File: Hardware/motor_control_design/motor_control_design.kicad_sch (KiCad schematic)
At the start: 78 parts, among them J10 3V3, J2 SWD, J3 VBAT, J4 GND, J5 FC_M/P, J6 Conn_01x06, J8 Conn_01x06, J9 GND, Q1 RF1S9540SM, Q10 2N7002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

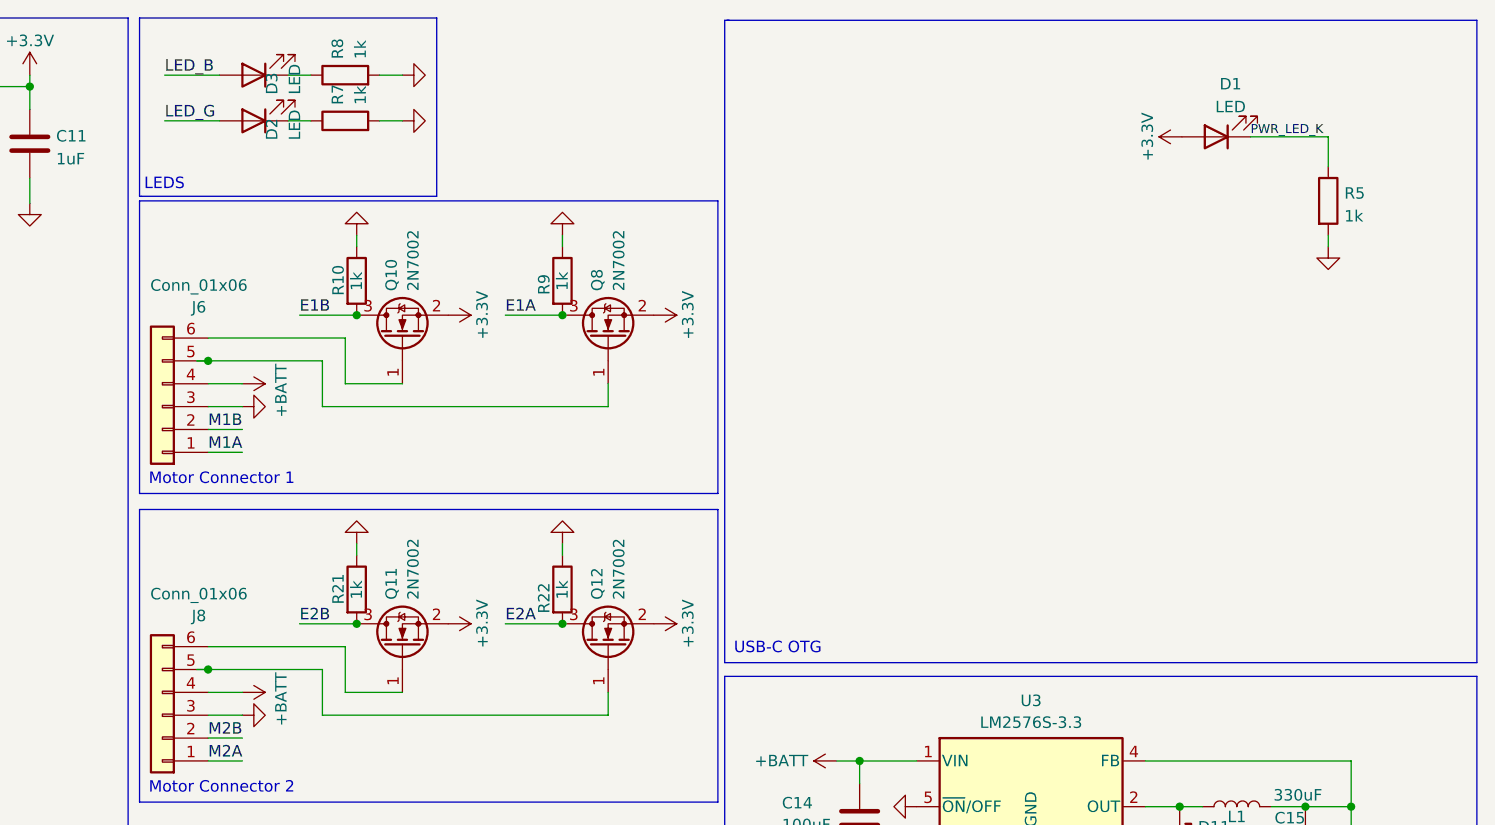
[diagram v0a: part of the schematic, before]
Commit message: Cleaned up motor board schema
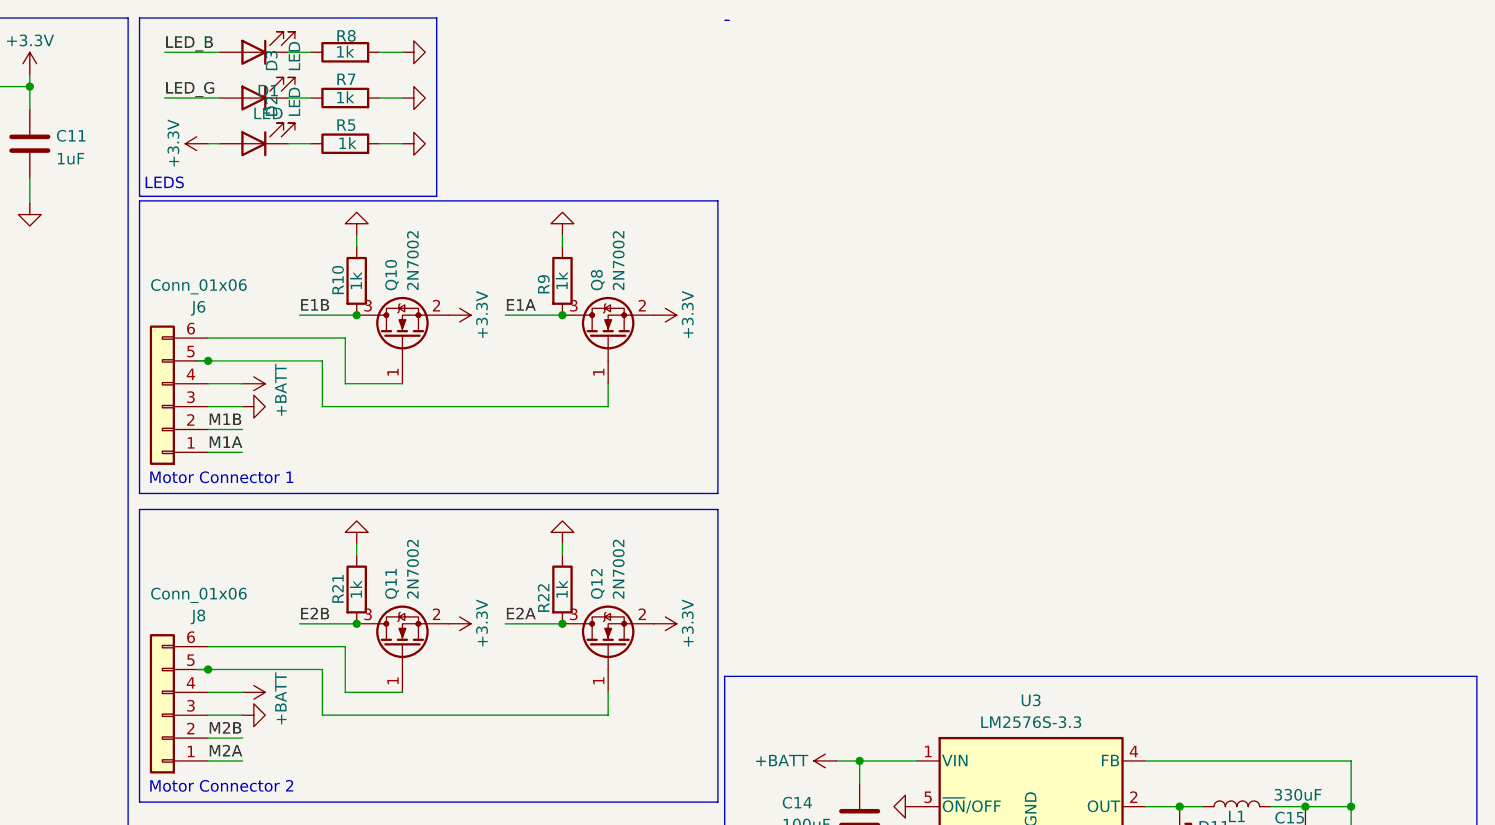
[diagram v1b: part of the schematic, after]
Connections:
- net PWR_LED_K: no longer names the net of D1.1 (K), R5.1
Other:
- note removed: "USB-C OTG"
- moved on the sheet: D1, D2, D3, R5, R7, R8

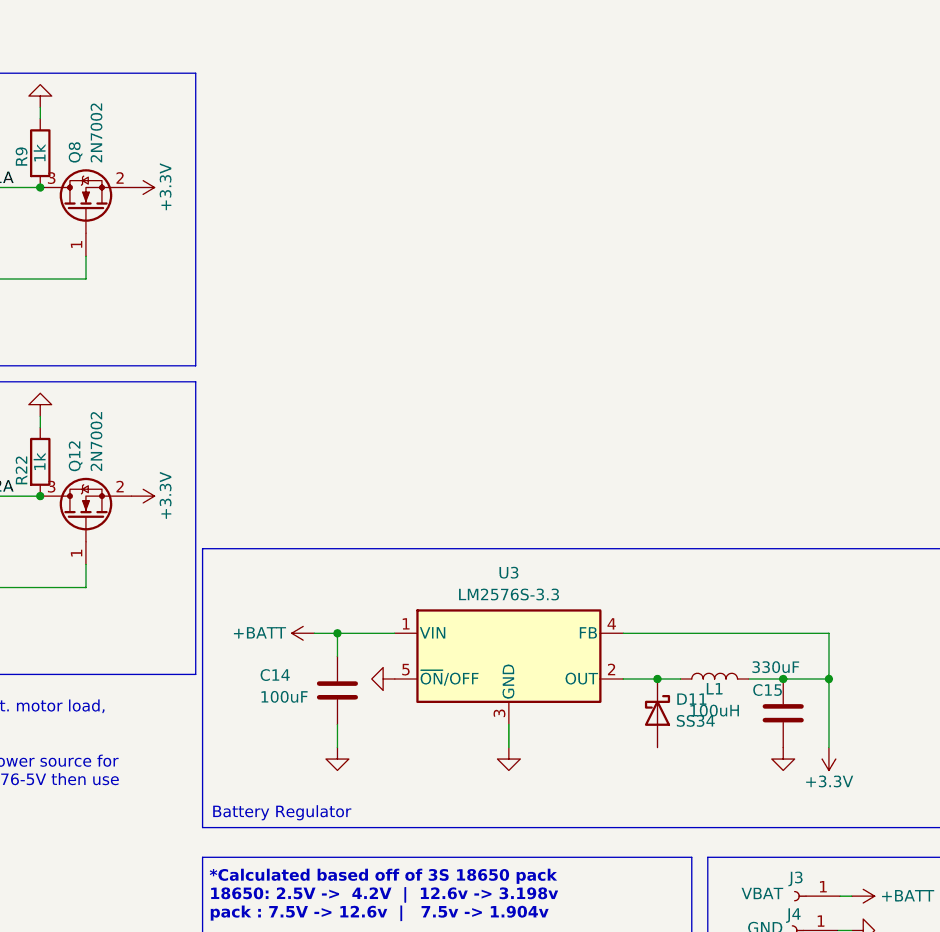
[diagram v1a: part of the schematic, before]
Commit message: Motor Board: Added LCSC Part Numbers Fixed missing ground on diode
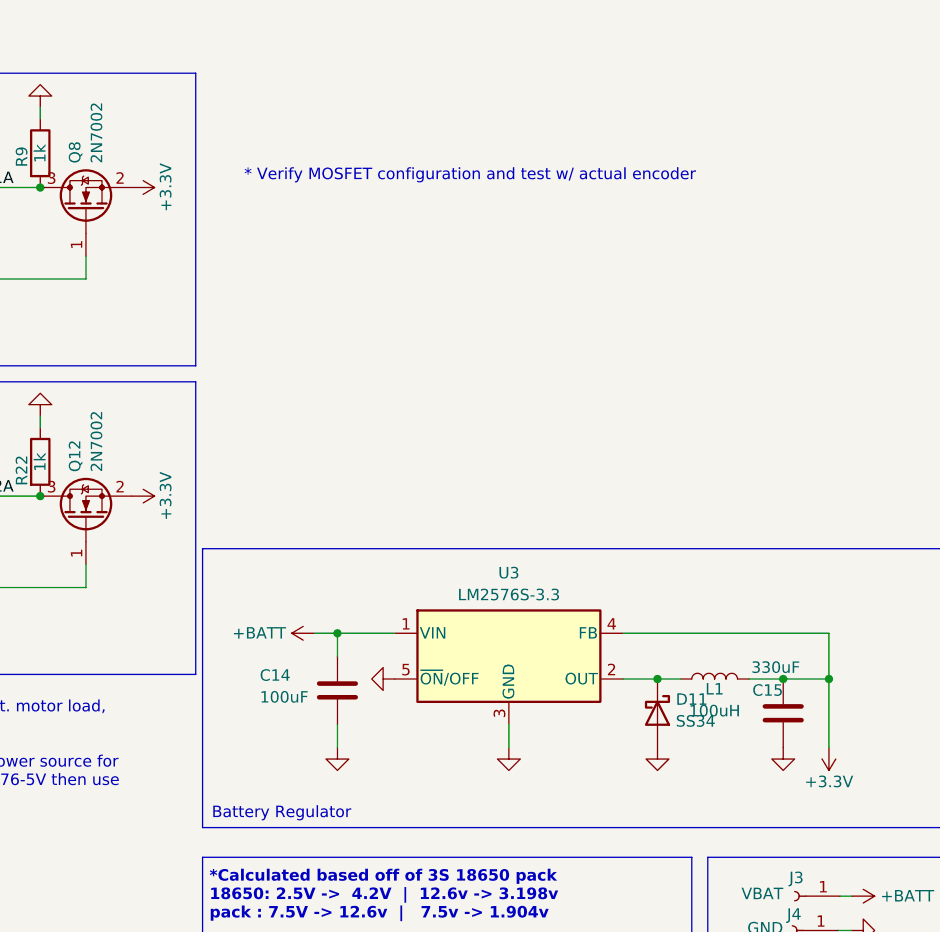
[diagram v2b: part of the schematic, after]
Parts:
- J5: LCSC Part (none) -> C124378
- Q1, Q14, Q2, Q6: LCSC Part (none) -> C33903
- Q10, Q11, Q12, Q13, Q16, Q4, Q5, Q8: LCSC Part (none) -> C466660
- Q15, Q3, Q7, Q9: LCSC Part (none) -> C538199
- R1, R2: LCSC Part C25906 -> C174364
- R10, R21, R22, R5, R7, R8, R9: LCSC Part C11702 -> C102758
- R11: LCSC Part C25906 -> C162880
- R12: LCSC Part C25906 -> C176114
- R13, R14, R15, R16, R17, R18, R19, R20, R23, R24, R4, R6: LCSC Part C60490 -> C102758
- R3: LCSC Part C60490 -> C176114
- U3: LCSC Part (none) -> C347414
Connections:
- net GND: now also D11.2 (A)
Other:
- note added: "* Verify MOSFET configuration and test w/ actual encoder"

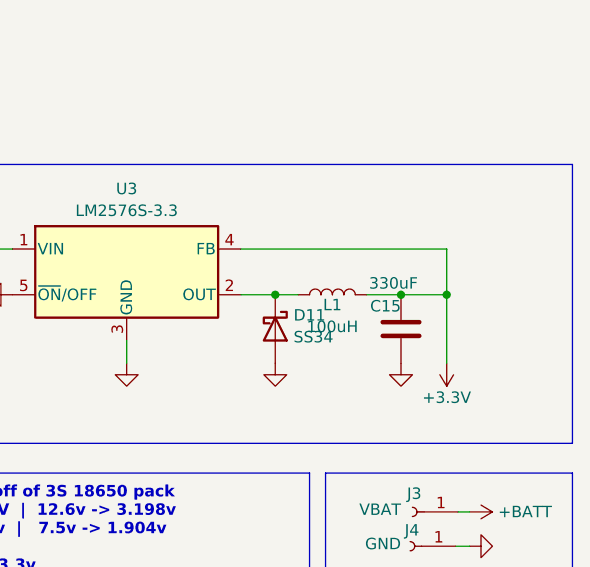
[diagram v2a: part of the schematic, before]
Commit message: Motor Board: Optimized LM2576 circuit - bigger capacitor - better inductor Added assembly files (outdated)
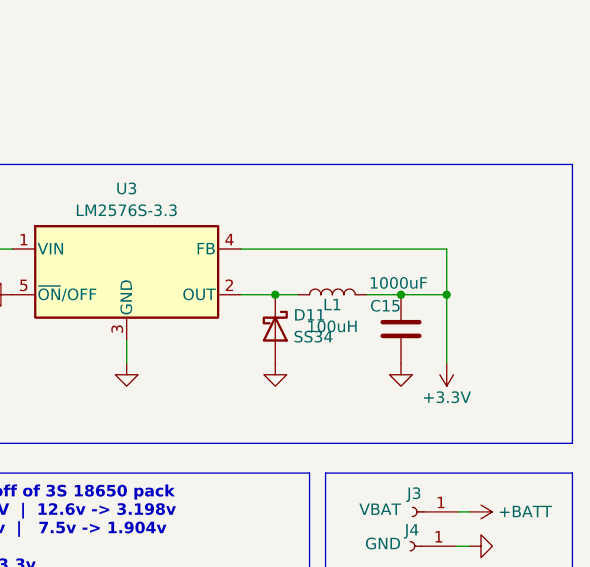
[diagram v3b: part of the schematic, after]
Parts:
- C14: footprint Capacitor_SMD:C_0603_1608Metric -> Capacitor_SMD:C_0805_2012Metric; LCSC Part C19702 -> C141660
- C15: value 330uF -> 1000uF; footprint Capacitor_SMD:C_0402_1005Metric -> Capacitor_SMD:CP_Elec_10x10.5; LCSC Part C19702 -> C189257
- D1: LCSC Part C273598 -> C2286
- D10, D11, D12, D4, D5, D6, D7, D8, D9: LCSC Part (none) -> C3032484
- D2: LCSC Part C273598 -> C779453
- D3: LCSC Part C273598 -> C131286
- J5: LCSC Part C124378 -> C132510
- L1: footprint Inductor_SMD:L_12x12mm_H4.5mm -> Inductor_SMD:L_TaiTech_TMPC1265_13.5x12.5mm; LCSC Part (none) -> C408533
- U3: LCSC Part C347414 -> C347412
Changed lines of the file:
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@@
 			)
 		)
+		(property "LCSC Part" "C3032484"
+			(at 124.46 153.67 90)
+			(effects
+				(font
+					(size 1.27 1.27)
+				)
+				(hide yes)
+			)
+		)
 		(pin "1"
 		)
@@
 			)
 		)
-		(property "LCSC Part" "C124378"
+		(property "LCSC Part" "C132510"
 			(at 275.59 148.59 0)
 			(effects
@@
 			)
 		)
-		(property "LCSC Part" "C273598"
+		(property "LCSC Part" "C2286"
 			(at 146.05 27.94 0)
 			(effects
@@
 			)
 		)
-		(property "Value" "330uF"
+		(property "Value" "1000uF"
 			(at 259.334 100.33 0)
 			(effects
@@
 			)
 		)
-		(property "Footprint" "Capacitor_SMD:C_0402_1005Metric"
+		(property "Footprint" "Capacitor_SMD:CP_Elec_10x10.5"
 			(at 263.8552 101.6 0)
 			(effects
@@
 			)
 		)
-		(property "LCSC Part" "C19702"
+		(property "LCSC Part" "C189257"
 			(at 262.89 105.41 0)
 			(effects
@@
 			)
 		)
+		(property "LCSC Part" "C3032484"
+			(at 59.69 166.37 90)
+			(effects
+				(font
+					(size 1.27 1.27)
+				)
+				(hide yes)
+			)
+		)
 		(pin "1"
 		)
@@
 			)
 		)
+		(property "LCSC Part" "C3032484"
+			(at 44.45 153.67 90)
+			(effects
+				(font
+					(size 1.27 1.27)
+				)
+				(hide yes)
+			)
+		)
 		(pin "1"
 		)
@@
 			)
 		)
+		(property "LCSC Part" "C3032484"
+			(at 124.46 166.37 90)
+			(effects
+				(font
+					(size 1.27 1.27)
+				)
+				(hide yes)
+			)
+		)
 		(pin "1"
 		)
@@
 			)
 		)
+		(property "LCSC Part" "C3032484"
+			(at 139.7 153.67 90)
+			(effects
+				(font
+					(size 1.27 1.27)
+				)
+				(hide yes)
+			)
+		)
 		(pin "1"
 		)
@@
 			)
 		)
+		(property "LCSC Part" "C3032484"
+			(at 44.45 166.37 90)
+			(effects
+				(font
+					(size 1.27 1.27)
+				)
+				(hide yes)
+			)
+		)
 		(pin "1"
 		)
@@
 			)
 		)
-		(property "Footprint" "Capacitor_SMD:C_0603_1608Metric"
+		(property "Footprint" "Capacitor_SMD:C_0805_2012Metric"
 			(at 212.3948 99.06 0)
 			(effects
@@
 			)
 		)
-		(property "LCSC Part" "C19702"
+		(property "LCSC Part" "C141660"
 			(at 213.36 102.87 0)
 			(effects
@@
 			)
 		)
+		(property "LCSC Part" "C3032484"
+			(at 248.92 105.41 90)
+			(effects
+				(font
+					(size 1.27 1.27)
+				)
+				(hide yes)
+			)
+		)
 		(pin "1"
 		)
@@
 			)
 		)
-		(property "Footprint" "Inductor_SMD:L_12x12mm_H4.5mm"
+		(property "Footprint" "Inductor_SMD:L_TaiTech_TMPC1265_13.5x12.5mm"
 			(at 255.27 101.6 0)
 			(effects
@@
 			)
 		)
+		(property "LCSC Part" "C408533"
+			(at 255.27 101.6 90)
+			(effects
+				(font
+					(size 1.27 1.27)
+				)
+				(hide yes)
+			)
+		)
 		(pin "1"
 		)
@@
 			)
 		)
+		(property "LCSC Part" "C3032484"
+			(at 59.69 153.67 90)
+			(effects
+				(font
+					(size 1.27 1.27)
+				)
+				(hide yes)
+			)
+		)
 		(pin "1"
 		)
@@
 			)
 		)
-		(property "LCSC Part" "C273598"
+		(property "LCSC Part" "C131286"
 			(at 146.05 17.78 0)
 			(effects
@@
 			)
 		)
-		(property "LCSC Part" "C273598"
+		(property "LCSC Part" "C779453"
 			(at 146.05 22.86 0)
 			(effects
@@
 			)
 		)
+		(property "LCSC Part" "C3032484"
+			(at 139.7 166.37 90)
+			(effects
+				(font
+					(size 1.27 1.27)
+				)
+				(hide yes)
+			)
+		)
 		(pin "1"
 		)
@@
 			)
 		)
-		(property "LCSC Part" "C347414"
+		(property "LCSC Part" " C347412"
 			(at 232.41 99.06 0)
 			(effects

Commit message: Added Via Stiching and ViPs to Motor Board
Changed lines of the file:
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@@
 	)
 	(junction
-		(at 22.86 115.57)
-		(diameter 0)
-		(color 0 0 0 0)
-	)
-	(junction
 		(at 44.45 148.59)
 		(diameter 0)
@@
 	(wire
 		(pts
-			(xy 22.86 115.57) (xy 22.86 118.11)
-		)
-		(stroke
-			(width 0)
-			(type default)
-		)
-	)
-	(wire
-		(pts
 			(xy 73.66 153.67) (xy 71.12 153.67)
 		)
@@
 	(wire
 		(pts
-			(xy 22.86 115.57) (xy 35.56 115.57)
-		)
-		(stroke
-			(width 0)
-			(type default)
-		)
-	)
-	(wire
-		(pts
 			(xy 100.33 97.79) (xy 107.95 97.79)
 		)
@@
 	(wire
 		(pts
-			(xy 22.86 111.76) (xy 22.86 115.57)
-		)
-		(stroke
-			(width 0)
-			(type default)
-		)
-	)
-	(wire
-		(pts
 			(xy 69.342 25.4) (xy 69.342 22.86)
 		)
@@
 		)
 	)
-	(wire
-		(pts
-			(xy 35.56 111.76) (xy 22.86 111.76)
-		)
-		(stroke
-			(width 0)
-			(type default)
-		)
-	)
 	(polyline
 		(pts
@@
 		)
 	)
-	(label "MOTOR_SDA"
-		(at 35.56 111.76 180)
-		(fields_autoplaced yes)
-		(effects
-			(font
-				(size 1.27 1.27)
-			)
-			(justify right bottom)
-		)
-	)
 	(label "SWCLK"
 		(at 107.95 113.03 180)
@@
 		)
 	)
-	(label "MOTOR_SCL"
-		(at 35.56 115.57 180)
-		(fields_autoplaced yes)
-		(effects
-			(font
-				(size 1.27 1.27)
-			)
-			(justify right bottom)
-		)
-	)
 	(label "E2A"
 		(at 107.95 92.71 180)
@@
 					(unit 1)
 				)
-			)
-		)
-	)
-	(symbol
-		(lib_name "+3.3V_1")
-		(lib_id "power:+3.3V")
-		(at 22.86 118.11 180)
-		(unit 1)
-		(exclude_from_sim no)
-		(in_bom yes)
-		(on_board yes)
-		(dnp no)
-		(fields_autoplaced yes)
-		(property "Reference" "#PWR02"
-			(at 22.86 114.3 0)
-			(effects
-				(font
-					(size 1.27 1.27)
-				)
-				(hide yes)
-			)
-		)
-		(property "Value" "+3.3V"
-			(at 22.86 122.2431 0)
-			(effects
-				(font
-					(size 1.27 1.27)
-				)
-			)
-		)
-		(property "Footprint" ""
-			(at 22.86 118.11 0)
-			(effects
-				(font
-					(size 1.27 1.27)
-				)
-				(hide yes)
-			)
-		)
-		(property "Datasheet" ""
-			(at 22.86 118.11 0)
-			(effects
-				(font
-					(size 1.27 1.27)
-				)
-				(hide yes)
-			)
-		)
-		(property "Description" "Power symbol creates a global label with name \"+3.3V\""
-			(at 22.86 118.11 0)
-			(effects
-				(font
-					(size 1.27 1.27)
-				)
-				(hide yes)
-			)
-		)
-		(pin "1"
-		)
-		(instances
-			(project "motor_control_design"
-				(path "/e96577c4-ec21-4b26-996c-9ebc38d9c737"
-					(reference "#PWR02")
-					(unit 1)
-				)
